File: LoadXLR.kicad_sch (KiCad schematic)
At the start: 23 parts, among them J1 NC3MAH, J2 NC3FAH2, J3 NC3MAH, J4 NC3FAH2, SW1 SW_DIP_x10

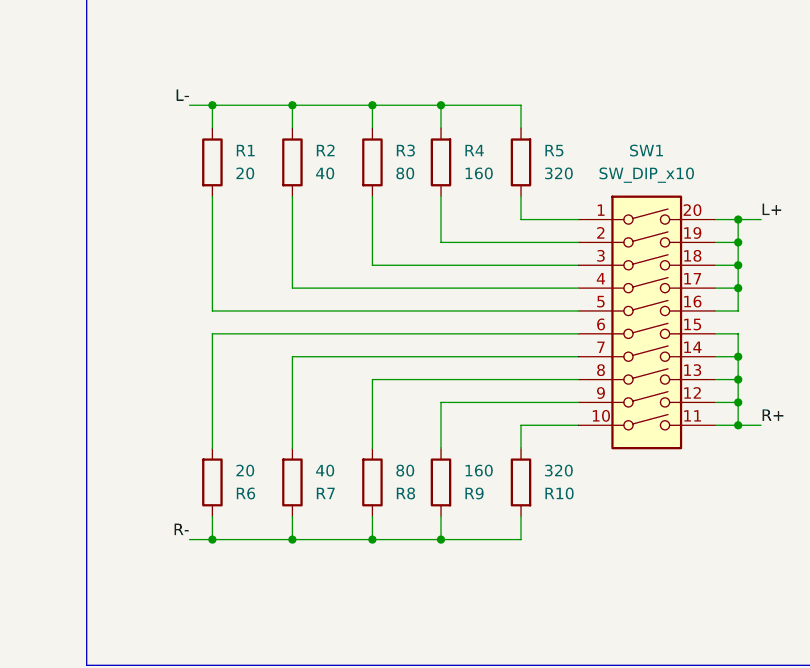
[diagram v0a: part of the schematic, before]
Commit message: Board layout
Updated the board layout.
Added a picture of the board render.
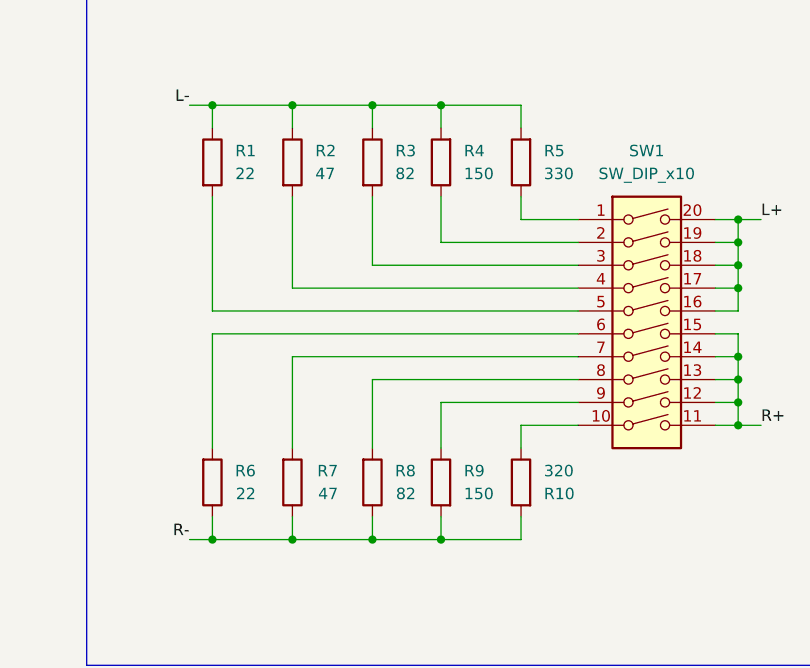
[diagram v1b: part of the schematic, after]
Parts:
- R1, R6: value 20 -> 22
- R2, R7: value 40 -> 47
- R3, R8: value 80 -> 82
- R4, R9: value 160 -> 150
- R5: value 320 -> 330
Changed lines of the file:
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@@
 		(on_board yes)
 		(dnp no)
-		(fields_autoplaced yes)
 		(property "Reference" "R7"
-			(at 186.69 106.6801 0)
-			(effects
-				(font
-					(size 1.27 1.27)
-				)
-				(justify left)
-			)
-		)
-		(property "Value" "40"
-			(at 186.69 104.1401 0)
-			(effects
-				(font
-					(size 1.27 1.27)
-				)
-				(justify left)
+			(at 189.23 104.14 0)
+			(effects
+				(font
+					(size 1.27 1.27)
+				)
+				(justify right)
+			)
+		)
+		(property "Value" "47"
+			(at 189.23 106.68 0)
+			(effects
+				(font
+					(size 1.27 1.27)
+				)
+				(justify right)
 			)
 		)
@@
 			)
 		)
-		(property "Value" "160"
+		(property "Value" "150"
 			(at 203.2 71.1199 0)
 			(effects
@@
 		(on_board yes)
 		(dnp no)
-		(fields_autoplaced yes)
 		(property "Reference" "R6"
-			(at 177.8 106.6801 0)
-			(effects
-				(font
-					(size 1.27 1.27)
-				)
-				(justify left)
-			)
-		)
-		(property "Value" "20"
-			(at 177.8 104.1401 0)
-			(effects
-				(font
-					(size 1.27 1.27)
-				)
-				(justify left)
+			(at 180.086 104.14 0)
+			(effects
+				(font
+					(size 1.27 1.27)
+				)
+				(justify right)
+			)
+		)
+		(property "Value" "22"
+			(at 180.086 106.68 0)
+			(effects
+				(font
+					(size 1.27 1.27)
+				)
+				(justify right)
 			)
 		)
@@
 			)
 		)
-		(property "Value" "320"
+		(property "Value" "330"
 			(at 212.09 71.1199 0)
 			(effects
@@
 		(fields_autoplaced yes)
 		(property "Reference" "R9"
-			(at 203.2 106.6801 0)
-			(effects
-				(font
-					(size 1.27 1.27)
-				)
-				(justify right)
-			)
-		)
-		(property "Value" "160"
-			(at 203.2 104.1401 0)
+			(at 203.2 104.1399 0)
+			(effects
+				(font
+					(size 1.27 1.27)
+				)
+				(justify right)
+			)
+		)
+		(property "Value" "150"
+			(at 203.2 106.6799 0)
 			(effects
 				(font
@@
 		(on_board yes)
 		(dnp no)
-		(fields_autoplaced yes)
 		(property "Reference" "R8"
-			(at 195.58 106.6801 0)
-			(effects
-				(font
-					(size 1.27 1.27)
-				)
-				(justify left)
-			)
-		)
-		(property "Value" "80"
-			(at 195.58 104.1401 0)
-			(effects
-				(font
-					(size 1.27 1.27)
-				)
-				(justify left)
+			(at 197.866 104.14 0)
+			(effects
+				(font
+					(size 1.27 1.27)
+				)
+				(justify right)
+			)
+		)
+		(property "Value" "82"
+			(at 197.866 106.68 0)
+			(effects
+				(font
+					(size 1.27 1.27)
+				)
+				(justify right)
 			)
 		)
@@
 			)
 		)
-		(property "Value" "20"
+		(property "Value" "22"
 			(at 177.8 71.1199 0)
 			(effects
@@
 			)
 		)
-		(property "Value" "40"
+		(property "Value" "47"
 			(at 186.69 71.1199 0)
 			(effects
@@
 			)
 		)
-		(property "Value" "80"
+		(property "Value" "82"
 			(at 195.58 71.1199 0)
 			(effects
